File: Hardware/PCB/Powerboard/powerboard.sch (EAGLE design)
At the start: 13 parts, among them IC1 TP4056, U1 TLV70033DDCT

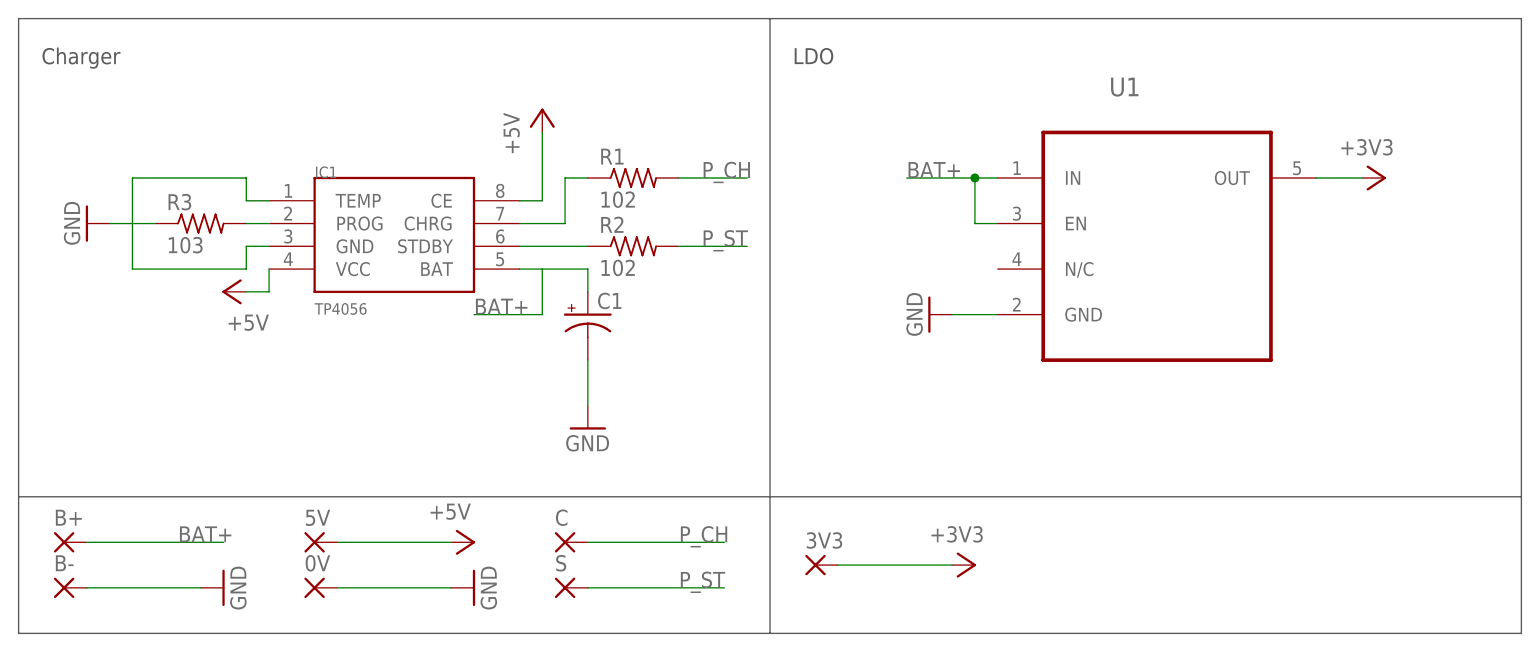
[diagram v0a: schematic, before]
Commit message: cloud push
- PCB size & pattern modified
- Enclosure minor fix
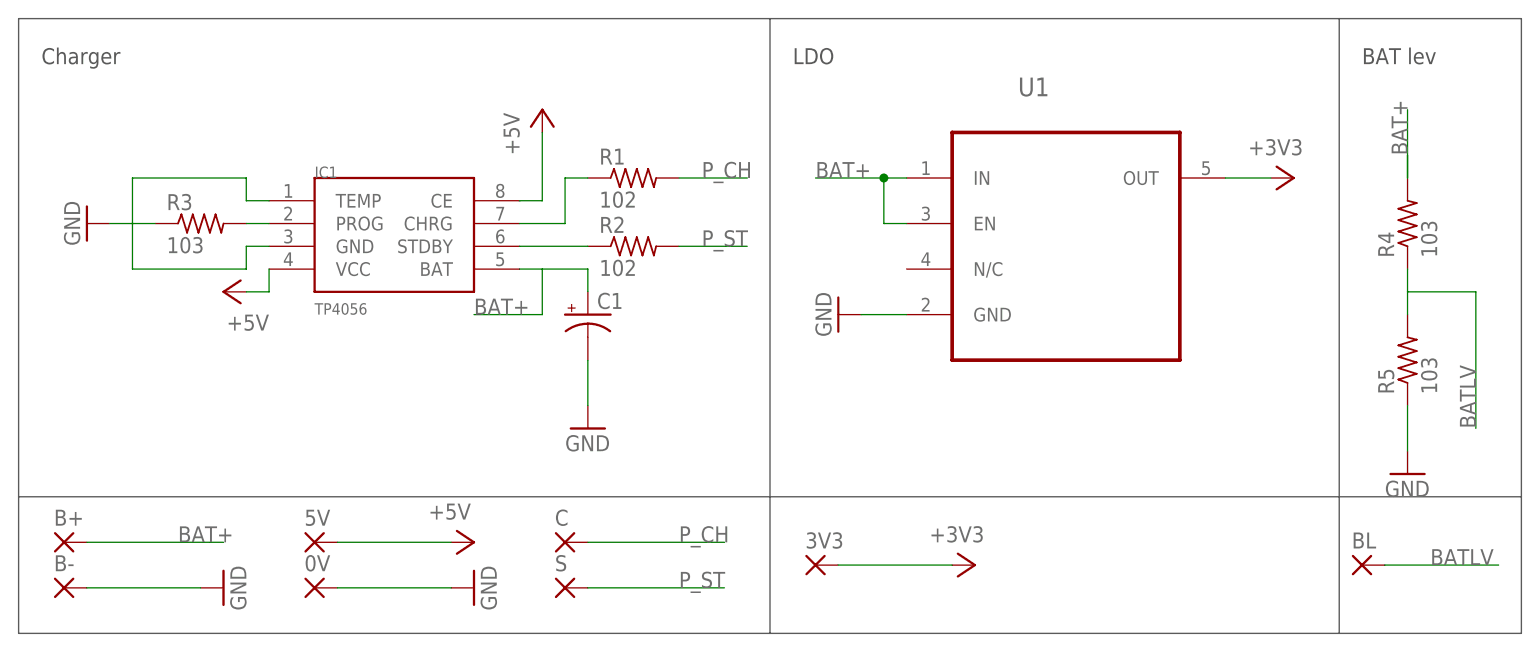
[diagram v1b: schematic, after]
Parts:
- added BL: (no value), wirepad:SMD5
- added R4, R5: 103, rcl:R-US_M2012
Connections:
- new net BATLV: BL.P, R4.1, R5.2
- net BAT+: now also R4.2
- net GND: now also R5.1
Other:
- note added: "BAT lev"
- moved on the sheet: U1
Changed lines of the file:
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@@
 <?xml version="1.0" encoding="utf-8"?>
 <!DOCTYPE eagle SYSTEM "eagle.dtd">
-<eagle version="8.0.0">
+<eagle version="8.0.2">
 <drawing>
 <settings>
@@
 <part name="3V3" library="wirepad" deviceset="SMD5" device=""/>
 <part name="+3V2" library="supply1" deviceset="+3V3" device=""/>
+<part name="R4" library="rcl" deviceset="R-US_" device="M2012" value="103"/>
+<part name="R5" library="rcl" deviceset="R-US_" device="M2012" value="103"/>
+<part name="GND6" library="supply1" deviceset="GND" device=""/>
+<part name="BL" library="wirepad" deviceset="SMD5" device=""/>
 </parts>
 <sheets>
 <sheet>
 <plain>
-<wire x1="83.82" y1="10.16" x2="167.64" y2="10.16" width="0.1524" layer="97"/>
+<wire x1="83.82" y1="10.16" x2="147.32" y2="10.16" width="0.1524" layer="97"/>
+<wire x1="147.32" y1="10.16" x2="167.64" y2="10.16" width="0.1524" layer="97"/>
 <wire x1="167.64" y1="10.16" x2="167.64" y2="25.4" width="0.1524" layer="97"/>
 <wire x1="167.64" y1="25.4" x2="167.64" y2="78.74" width="0.1524" layer="97"/>
-<wire x1="167.64" y1="78.74" x2="83.82" y2="78.74" width="0.1524" layer="97"/>
+<wire x1="167.64" y1="78.74" x2="147.32" y2="78.74" width="0.1524" layer="97"/>
+<wire x1="147.32" y1="78.74" x2="83.82" y2="78.74" width="0.1524" layer="97"/>
 <wire x1="83.82" y1="78.74" x2="0" y2="78.74" width="0.1524" layer="97"/>
 <wire x1="0" y1="78.74" x2="0" y2="25.4" width="0.1524" layer="97"/>
@@
 <text x="86.36" y="73.66" size="1.778" layer="97">LDO</text>
 <wire x1="0" y1="25.4" x2="167.64" y2="25.4" width="0.1524" layer="97"/>
+<wire x1="147.32" y1="78.74" x2="147.32" y2="10.16" width="0.1524" layer="97"/>
+<text x="149.86" y="73.66" size="1.778" layer="97">BAT lev</text>
 </plain>
 <instances>
@@
 <instance part="R1" gate="G$1" x="68.58" y="60.96"/>
 <instance part="R2" gate="G$1" x="68.58" y="53.34"/>
-<instance part="U1" gate="A" x="127" y="55.88"/>
-<instance part="+3V1" gate="G$1" x="152.4" y="60.96" rot="R270"/>
-<instance part="GND1" gate="1" x="101.6" y="45.72" rot="R270"/>
+<instance part="U1" gate="A" x="116.84" y="55.88"/>
+<instance part="+3V1" gate="G$1" x="142.24" y="60.96" rot="R270"/>
+<instance part="GND1" gate="1" x="91.44" y="45.72" rot="R270"/>
 <instance part="P+1" gate="1" x="22.86" y="48.26" rot="R90"/>
 <instance part="P+2" gate="1" x="58.42" y="68.58"/>
@@
 <instance part="3V3" gate="1" x="88.9" y="17.78"/>
 <instance part="+3V2" gate="G$1" x="106.68" y="17.78" rot="R270"/>
+<instance part="R4" gate="G$1" x="154.94" y="55.88" rot="R90"/>
+<instance part="R5" gate="G$1" x="154.94" y="40.64" rot="R90"/>
+<instance part="GND6" gate="1" x="154.94" y="27.94"/>
+<instance part="BL" gate="1" x="149.86" y="17.78"/>
 </instances>
 <busses>
@@
 <pinref part="U1" gate="A" pin="GND"/>
 <pinref part="GND1" gate="1" pin="GND"/>
-<wire x1="104.14" y1="45.72" x2="109.22" y2="45.72" width="0.1524" layer="91"/>
+<wire x1="93.98" y1="45.72" x2="99.06" y2="45.72" width="0.1524" layer="91"/>
 </segment>
 <segment>
@@
 <wire x1="35.56" y1="15.24" x2="48.26" y2="15.24" width="0.1524" layer="91"/>
 <pinref part="GND5" gate="1" pin="GND"/>
+</segment>
+<segment>
+<pinref part="R5" gate="G$1" pin="1"/>
+<wire x1="154.94" y1="35.56" x2="154.94" y2="30.48" width="0.1524" layer="91"/>
+<pinref part="GND6" gate="1" pin="GND"/>
 </segment>
 </net>
@@
 <segment>
 <pinref part="U1" gate="A" pin="IN"/>
-<wire x1="109.22" y1="60.96" x2="106.68" y2="60.96" width="0.1524" layer="91"/>
-<label x="99.06" y="60.96" size="1.778" layer="95"/>
+<wire x1="99.06" y1="60.96" x2="96.52" y2="60.96" width="0.1524" layer="91"/>
+<label x="88.9" y="60.96" size="1.778" layer="95"/>
 <pinref part="U1" gate="A" pin="EN"/>
-<wire x1="106.68" y1="60.96" x2="99.06" y2="60.96" width="0.1524" layer="91"/>
-<wire x1="109.22" y1="55.88" x2="106.68" y2="55.88" width="0.1524" layer="91"/>
-<wire x1="106.68" y1="55.88" x2="106.68" y2="60.96" width="0.1524" layer="91"/>
-<junction x="106.68" y="60.96"/>
+<wire x1="96.52" y1="60.96" x2="88.9" y2="60.96" width="0.1524" layer="91"/>
+<wire x1="99.06" y1="55.88" x2="96.52" y2="55.88" width="0.1524" layer="91"/>
+<wire x1="96.52" y1="55.88" x2="96.52" y2="60.96" width="0.1524" layer="91"/>
+<junction x="96.52" y="60.96"/>
 </segment>
 <segment>
@@
 <label x="17.78" y="20.32" size="1.778" layer="95"/>
 </segment>
+<segment>
+<pinref part="R4" gate="G$1" pin="2"/>
+<wire x1="154.94" y1="60.96" x2="154.94" y2="63.5" width="0.1524" layer="91"/>
+<wire x1="154.94" y1="60.96" x2="154.94" y2="68.58" width="0.1524" layer="91"/>
+<label x="154.94" y="63.5" size="1.778" layer="95" rot="R90"/>
+</segment>
 </net>
 <net name="N$3" class="0">
@@
 <pinref part="U1" gate="A" pin="OUT"/>
 <pinref part="+3V1" gate="G$1" pin="+3V3"/>
-<wire x1="149.86" y1="60.96" x2="144.78" y2="60.96" width="0.1524" layer="91"/>
+<wire x1="139.7" y1="60.96" x2="134.62" y2="60.96" width="0.1524" layer="91"/>
 </segment>
 <segment>
@@
 </segment>
 </net>
+<net name="BATLV" class="0">
+<segment>
+<wire x1="152.4" y1="17.78" x2="165.1" y2="17.78" width="0.1524" layer="91"/>
+<pinref part="BL" gate="1" pin="P"/>
+<label x="157.48" y="17.78" size="1.778" layer="95"/>
+</segment>
+<segment>
+<pinref part="R4" gate="G$1" pin="1"/>
+<wire x1="154.94" y1="50.8" x2="154.94" y2="48.26" width="0.1524" layer="91"/>
+<pinref part="R5" gate="G$1" pin="2"/>
+<wire x1="154.94" y1="48.26" x2="154.94" y2="45.72" width="0.1524" layer="91"/>
+<wire x1="154.94" y1="48.26" x2="162.56" y2="48.26" width="0.1524" layer="91"/>
+<wire x1="162.56" y1="48.26" x2="162.56" y2="33.02" width="0.1524" layer="91"/>
+<label x="162.56" y="33.02" size="1.778" layer="95" rot="R90"/>
+</segment>
+</net>
